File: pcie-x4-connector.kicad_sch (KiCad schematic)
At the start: 0 parts

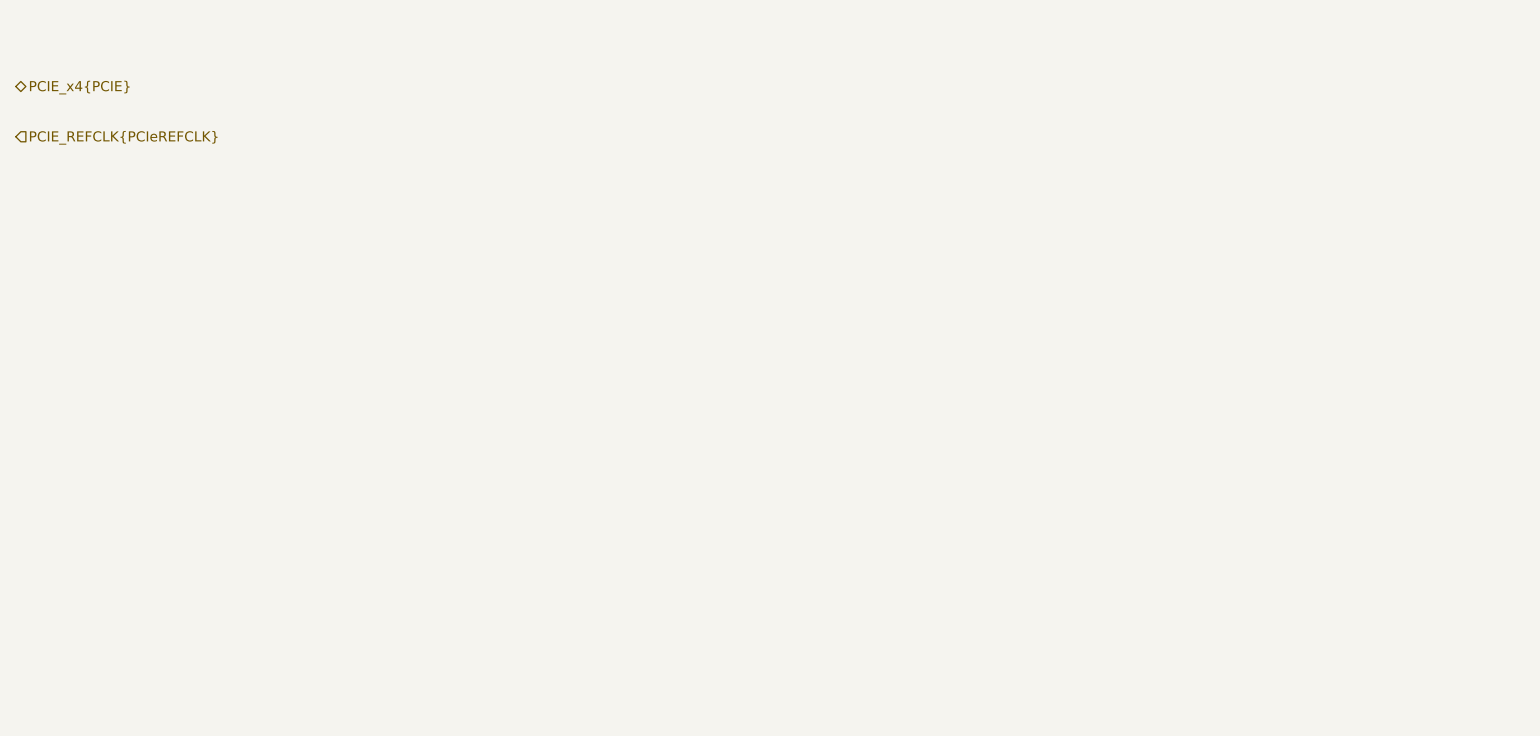
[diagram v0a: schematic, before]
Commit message: Add PCIe x4 connector (M.2 key M)
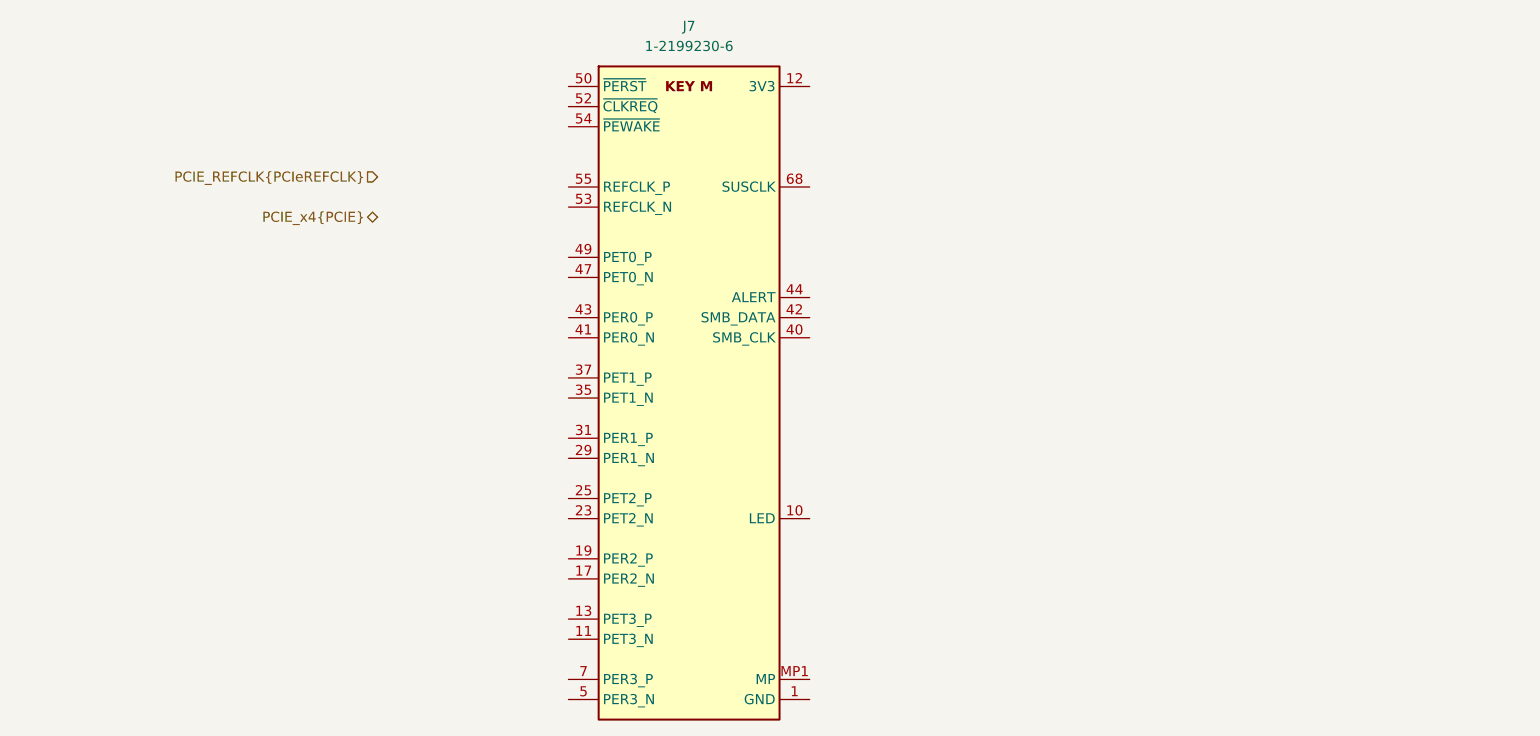
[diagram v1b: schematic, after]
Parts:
- added J7: Bus_M.2_1-2199230-6, antmicro-footprints:Bus_M.2_Socket_Key_M_TE_1-2199230-6, symbol antmicroPciConnectors:Bus_M.2_1-2199230-6
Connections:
- new net: J7.1 (GND), J7.15 (GND), J7.21 (GND), J7.27 (GND), J7.3 (GND), J7.33 (GND), J7.39 (GND), J7.45 (GND), J7.51 (GND), J7.57 (GND), J7.71 (GND), J7.73 (GND), J7.75 (GND), J7.9 (GND)
- new net: J7.12 (3V3), J7.14 (3V3), J7.16 (3V3), J7.18 (3V3), J7.2 (3V3), J7.4 (3V3), J7.70 (3V3), J7.72 (3V3), J7.74 (3V3)
- new net: J7.MP1 (MP), J7.MP2 (MP)

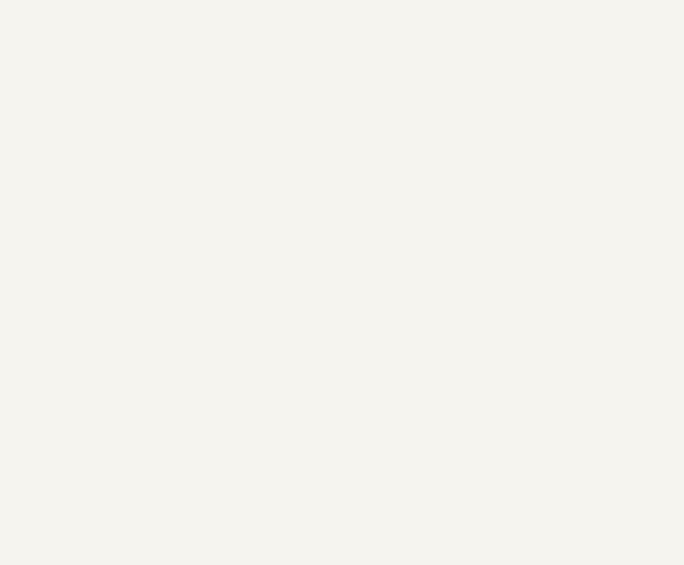
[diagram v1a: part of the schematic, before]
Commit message: [#82176] Add M.2 and TPM connectors
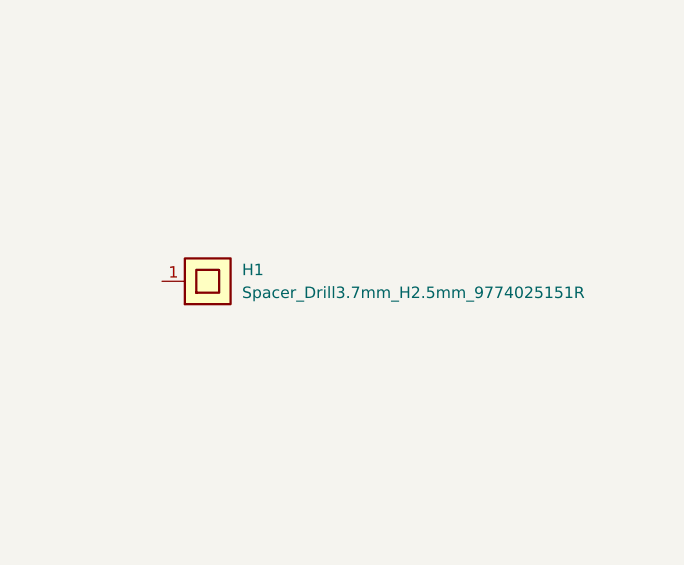
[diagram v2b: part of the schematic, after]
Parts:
- added H1: Spacer_Drill3.7mm_H2.5mm_9774025151R, antmicro-footprints:Spacer_Drill3.7mm_H2.5mm_9774025151R, symbol antmicroMechanicalParts:Spacer_Drill3.7mm_H2.5mm_9774025151R
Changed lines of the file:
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@@
+	)
+	(symbol
+		(lib_id "antmicroMechanicalParts:Spacer_Drill3.7mm_H2.5mm_9774025151R")
+		(at 257.81 119.38 0)
+		(unit 1)
+		(exclude_from_sim no)
+		(in_bom yes)
+		(on_board yes)
+		(dnp no)
+		(fields_autoplaced yes)
+		(property "Reference" "H1"
+			(at 266.7 118.11 0)
+			(effects
+				(font
+					(size 1.27 1.27)
+					(thickness 0.15)
+				)
+				(justify left)
+			)
+		)
+		(property "Value" "Spacer_Drill3.7mm_H2.5mm_9774025151R"
+			(at 266.7 120.65 0)
+			(effects
+				(font
+					(size 1.27 1.27)
+					(thickness 0.15)
+				)
+				(justify left)
+			)
+		)
+		(property "Footprint" "antmicro-footprints:Spacer_Drill3.7mm_H2.5mm_9774025151R"
+			(at 280.67 127 0)
+			(effects
+				(font
+					(size 1.27 1.27)
+					(thickness 0.15)
+				)
+				(justify left bottom)
+				(hide yes)
+			)
+		)
+		(property "Datasheet" "https://www.we-online.com/components/products/datasheet/9774025151R.pdf"
+			(at 280.67 129.54 0)
+			(effects
+				(font
+					(size 1.27 1.27)
+					(thickness 0.15)
+				)
+				(justify left bottom)
+				(hide yes)
+			)
+		)
+		(property "Description" "Spacer, SMT, Non Stop, Steel, Swage Round, 5.1 mm x 2.5 mm, M2.5 Thread, WA-SMSI Series"
+			(at 257.81 119.38 0)
+			(effects
+				(font
+					(size 1.27 1.27)
+				)
+				(hide yes)
+			)
+		)
+		(property "Manufacturer" "Würth Elektronik"
+			(at 280.67 132.08 0)
+			(effects
+				(font
+					(size 1.27 1.27)
+					(thickness 0.15)
+				)
+				(justify left bottom)
+				(hide yes)
+			)
+		)
+		(property "MPN" "9774025151R"
+			(at 280.67 134.62 0)
+			(effects
+				(font
+					(size 1.27 1.27)
+					(thickness 0.15)
+				)
+				(justify left bottom)
+				(hide yes)
+			)
+		)
+		(property "Author" "Antmicro"
+			(at 280.67 137.16 0)
+			(effects
+				(font
+					(size 1.27 1.27)
+					(thickness 0.15)
+				)
+				(justify left bottom)
+				(hide yes)
+			)
+		)
+		(property "License" "Apache-2.0"
+			(at 280.67 139.7 0)
+			(effects
+				(font
+					(size 1.27 1.27)
+					(thickness 0.15)
+				)
+				(justify left bottom)
+				(hide yes)
+			)
+		)
+		(pin "1"
+		)
+		(instances
+			(project ""
+				(path "/5f636c45-3c15-4731-8931-4625e0dab7e4/945730c0-5d04-4966-88eb-4ee840f8c440"
+					(reference "H1")
+					(unit 1)
+				)
+			)
+		)
 	)
 	(symbol
